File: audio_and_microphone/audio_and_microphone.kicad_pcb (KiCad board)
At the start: 2 copper layers, 14 parts

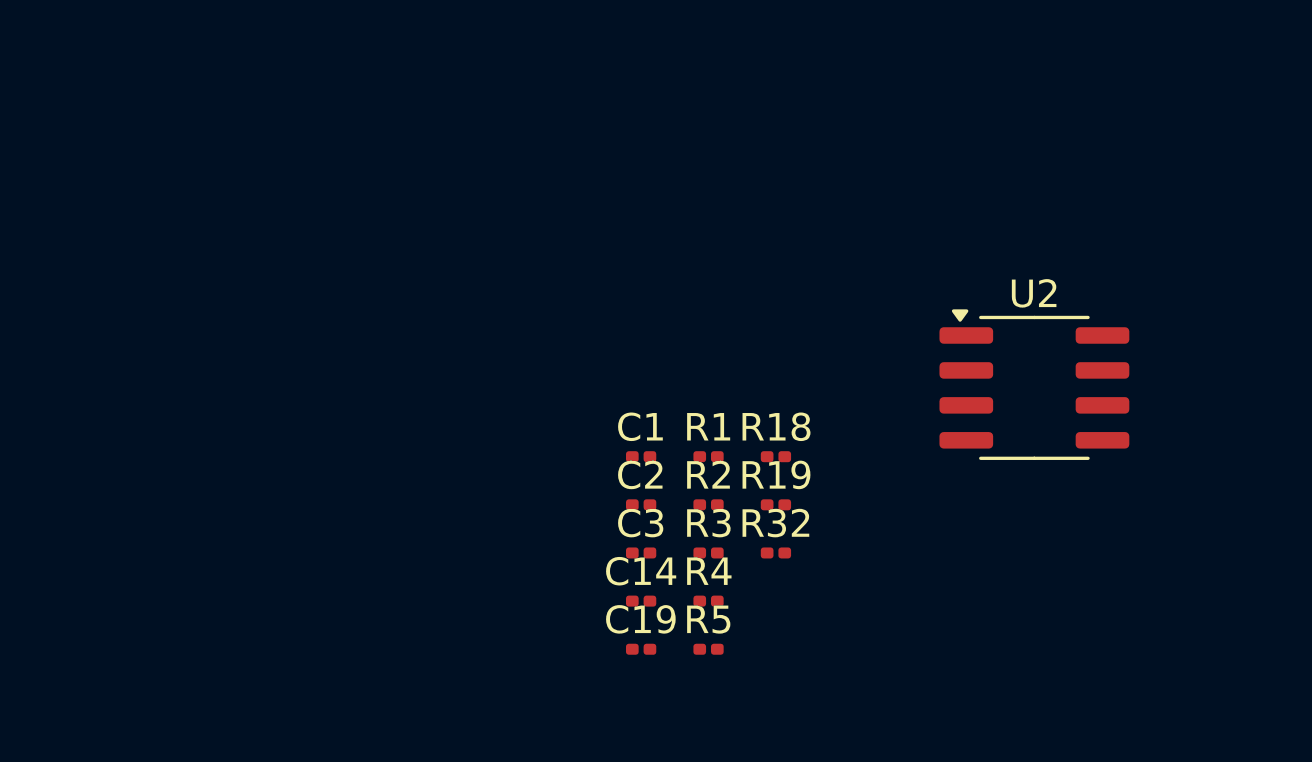
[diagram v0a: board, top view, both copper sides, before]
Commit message: updated footprints and pcb layout without 3.3 V connection
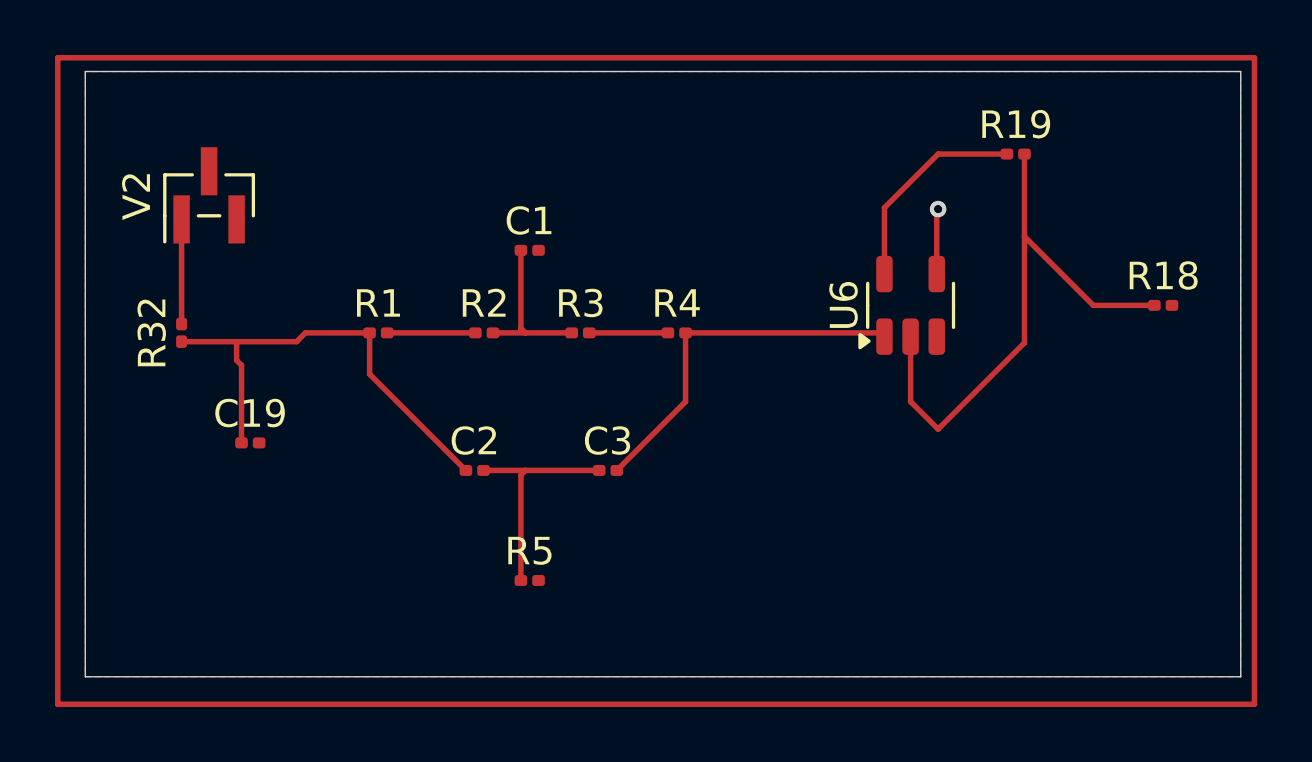
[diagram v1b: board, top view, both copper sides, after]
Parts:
- removed C14: 0.1u, Capacitor_SMD:C_0201_0603Metric
- removed U2: ~, Package_SO:SOIC-8_3.9x4.9mm_P1.27mm
- added U6: ~, Package_TO_SOT_SMD:SOT-23-5, F.Cu at (141.5, 55.5)
- added V2: VPWL, Connector_PinHeader_1.00mm:PinHeader_1x03_P1.00mm_Vertical_SMD_Pin1Left, F.Cu at (116.0, 51.5)
- moved R32 23.0 mm to (115.0, 56.5), turned to 90 degrees
- moved C19 16.1 mm to (117.5, 60.5)
- moved R19 15.4 mm to (145.3, 50.0)
- moved R18 15.1 mm to (150.7, 55.5)
- moved R1 12.8 mm to (122.2, 56.5)
- moved R2 10.3 mm to (126.0, 56.5)
- moved R4 9.82 mm to (133.0, 56.5)
- moved R3 9.26 mm to (129.5, 56.5)
- moved C1 8.52 mm to (127.7, 53.5)
- moved R5 6.96 mm to (127.7, 65.5)
- moved C2 6.18 mm to (125.7, 61.5)
- moved C3 3.23 mm to (130.5, 61.5)
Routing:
- net Net-(U6--): track 0.00 -> 20.8 mm
- net Net-(C19-Pad1): track 0.00 -> 17.2 mm
- net Net-(U6-+): track 0.00 -> 13.3 mm
- net Net-(C2-Pad2): track 0.00 -> 8.27 mm
- net /ENV_OUT: track 0.00 -> 7.67 mm
- net Net-(C1-Pad1): track 0.00 -> 5.93 mm
- net Net-(R32-Pad2): track 0.00 -> 3.80 mm
- net Net-(R1-Pad2): track 0.00 -> 3.21 mm
- net Net-(R3-Pad2): track 0.00 -> 2.86 mm
- net GND: track 0.00 -> 2.38 mm, vias 0 -> 1
- added copper zone on F.Cu, net GND
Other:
- board outline added: 42 x 22 mm

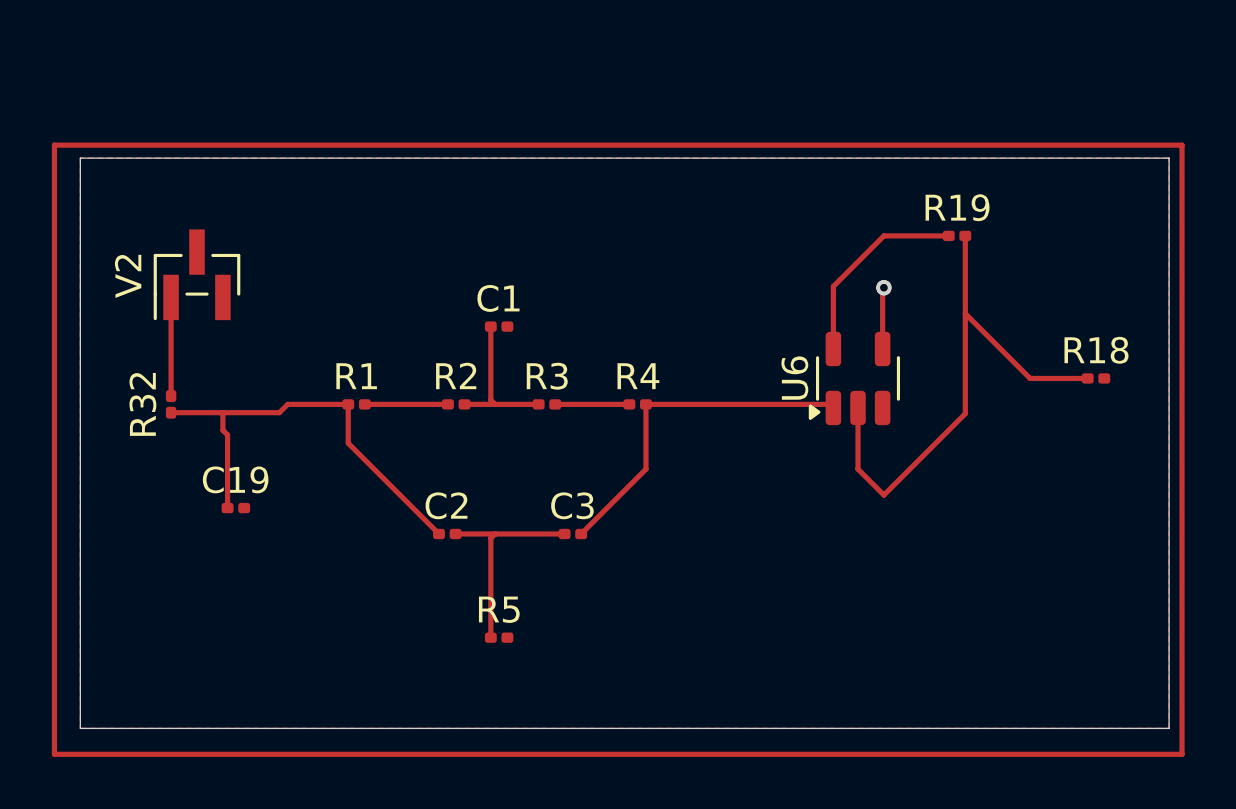
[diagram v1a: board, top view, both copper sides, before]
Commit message: improved pcb space layout
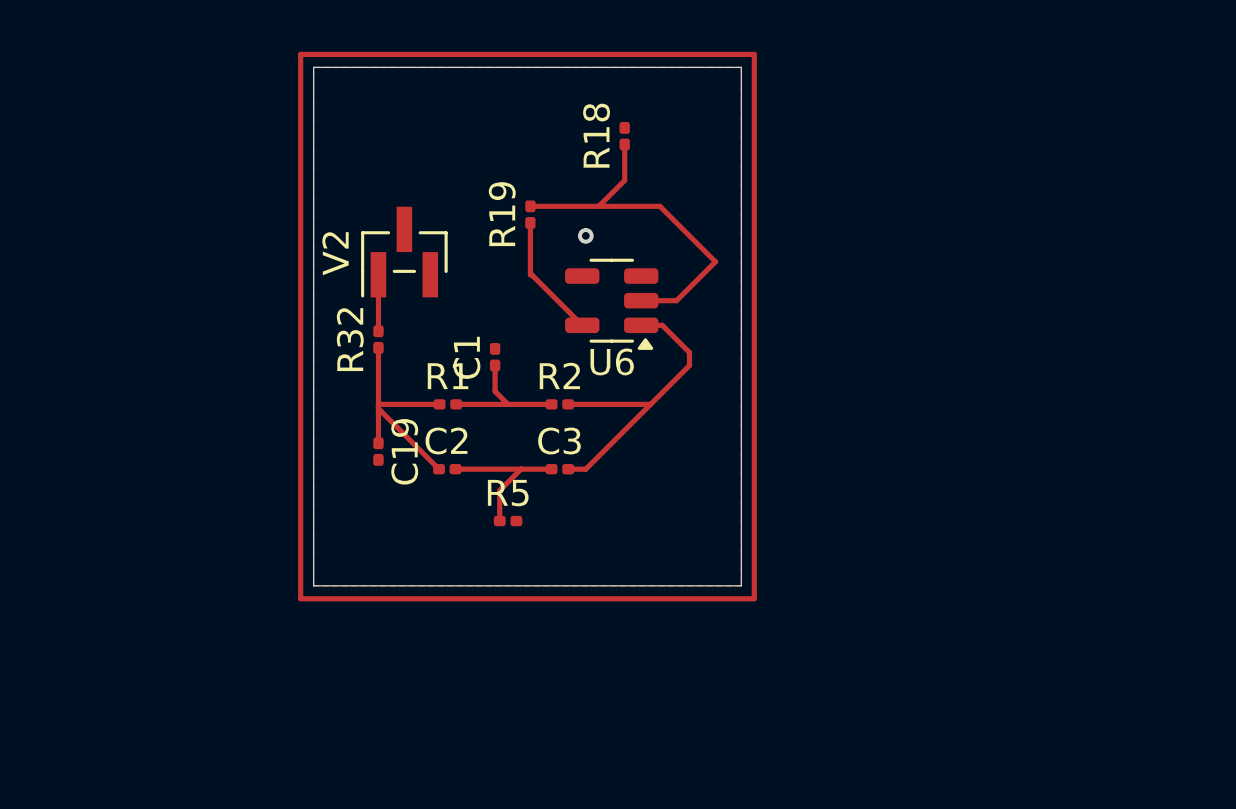
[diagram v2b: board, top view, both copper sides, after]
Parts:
- removed the R2 at (126.0, 56.5)
- removed R3: 4.7k, Resistor_SMD:R_0201_0603Metric
- R1: value 4.7k -> 26.7k
- R2: renamed from R4; value 22k -> 26.7k
- moved R18 20.4 mm to (132.5, 46.2), turned to 90 degrees
- moved R19 16.5 mm to (128.9, 49.2), turned to 90 degrees
- moved U6 9.96 mm to (132.0, 52.5), turned to 180 degrees
- moved R32 8.38 mm to (123.0, 54.0)
- moved V2 8.05 mm to (124.0, 50.6)
- moved C19 5.92 mm to (123.0, 58.3), turned to -90 degrees
- moved R5 4.51 mm to (128.0, 61.0)
- moved R1 3.53 mm to (125.7, 56.5)
- moved R2 3.00 mm to (130.0, 56.5)
- moved C3 2.55 mm to (130.0, 59.0)
- moved C2 2.50 mm to (125.7, 59.0)
- moved C1 1.19 mm to (127.5, 54.7), turned to 90 degrees
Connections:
- R1 pad 2: Net-(R1-Pad2) -> Net-(C1-Pad1)
- R2 pad 1: Net-(R3-Pad2) -> Net-(C1-Pad1)
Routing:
- net Net-(C19-Pad1): track 17.2 -> 9.51 mm
- net Net-(U6--): track 20.8 -> 14.3 mm
- net Net-(R1-Pad2): track 3.21 -> 0.00 mm
- net /ENV_OUT: track 7.67 -> 4.81 mm
- net Net-(R3-Pad2): track 2.86 -> 0.00 mm
- net GND: track 2.38 -> 0.00 mm
- net Net-(C2-Pad2): track 8.27 -> 6.04 mm
- net Net-(R32-Pad2): track 3.80 -> 2.18 mm
- net Net-(U6-+): track 13.3 -> 12.3 mm
- net Net-(C1-Pad1): track 5.93 -> 5.39 mm
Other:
- board size 42 x 22 mm -> 16.5 x 20 mm

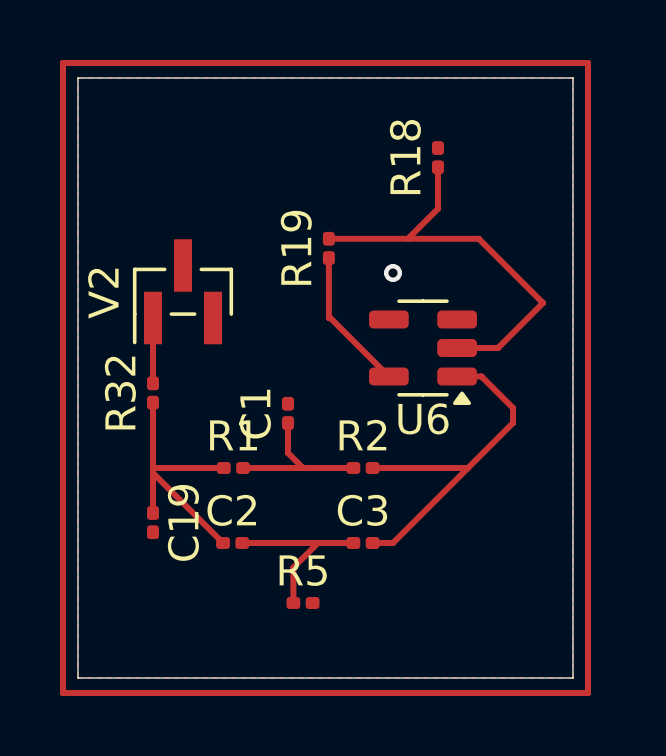
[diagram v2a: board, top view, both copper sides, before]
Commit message: excluded voltage sources from board and replaced with connectors
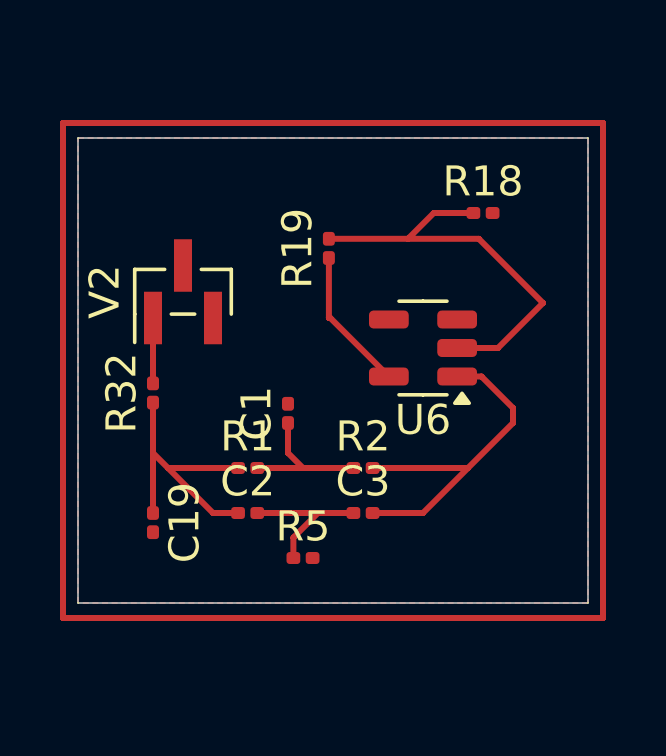
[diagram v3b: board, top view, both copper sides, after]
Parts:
- moved R18 2.38 mm to (134.0, 48.0), turned to 0 degrees
- moved R5 1.50 mm to (128.0, 59.5)
- moved C2 1.12 mm to (126.2, 58.0)
- moved C3 1.00 mm to (130.0, 58.0)
- moved R1 0.47 mm to (126.2, 56.5)
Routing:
- net Net-(C2-Pad2): track 6.04 -> 5.04 mm
- net GND: vias 1 -> 0
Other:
- board size 16.5 x 20 mm -> 17 x 15.5 mm
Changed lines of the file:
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@@
 	(footprint "Resistor_SMD:R_0201_0603Metric"
 		(layer "F.Cu")
-		(at 132.5 46.155 90)
+		(at 134 48)
 		(descr "Resistor SMD 0201 (0603 Metric), square (rectangular) end terminal, IPC-7351 nominal, (Body size source: https://www.vishay.com/docs/20052/crcw0201e3.pdf), generated with kicad-footprint-generator")
 		(tags "resistor")
 		(property "Reference" "R18"
-			(at 0 -1.05 90)
+			(at 0 -1.05 0)
 			(layer "F.SilkS")
 			(effects
@@
 		)
 		(property "Value" "22K"
-			(at 0 1.05 90)
+			(at 0 1.05 0)
 			(layer "F.Fab")
 			(effects
@@
 		)
 		(property "Datasheet" "~"
-			(at 0 0 90)
+			(at 0 0 0)
 			(layer "F.Fab")
 			(hide yes)
@@
 		)
 		(property "Description" "Resistor, US symbol"
-			(at 0 0 90)
+			(at 0 0 0)
 			(layer "F.Fab")
 			(hide yes)
@@
 		(attr smd)
 		(fp_line
+			(start -0.7 -0.35)
+			(end 0.7 -0.35)
+			(stroke
+				(width 0.05)
+				(type solid)
+			)
+			(layer "F.CrtYd")
+		)
+		(fp_line
+			(start -0.7 0.35)
+			(end -0.7 -0.35)
+			(stroke
+				(width 0.05)
+				(type solid)
+			)
+			(layer "F.CrtYd")
+		)
+		(fp_line
 			(start 0.7 -0.35)
 			(end 0.7 0.35)
@@
 		)
 		(fp_line
-			(start -0.7 -0.35)
-			(end 0.7 -0.35)
-			(stroke
-				(width 0.05)
-				(type solid)
-			)
-			(layer "F.CrtYd")
-		)
-		(fp_line
 			(start 0.7 0.35)
 			(end -0.7 0.35)
@@
 		)
 		(fp_line
-			(start -0.7 0.35)
-			(end -0.7 -0.35)
-			(stroke
-				(width 0.05)
-				(type solid)
-			)
-			(layer "F.CrtYd")
+			(start -0.3 -0.15)
+			(end 0.3 -0.15)
+			(stroke
+				(width 0.1)
+				(type solid)
+			)
+			(layer "F.Fab")
+		)
+		(fp_line
+			(start -0.3 0.15)
+			(end -0.3 -0.15)
+			(stroke
+				(width 0.1)
+				(type solid)
+			)
+			(layer "F.Fab")
 		)
 		(fp_line
@@
 		)
 		(fp_line
-			(start -0.3 -0.15)
-			(end 0.3 -0.15)
-			(stroke
-				(width 0.1)
-				(type solid)
-			)
-			(layer "F.Fab")
-		)
-		(fp_line
 			(start 0.3 0.15)
 			(end -0.3 0.15)
@@
 			(layer "F.Fab")
 		)
-		(fp_line
-			(start -0.3 0.15)
-			(end -0.3 -0.15)
-			(stroke
-				(width 0.1)
-				(type solid)
-			)
-			(layer "F.Fab")
-		)
 		(fp_text user "${REFERENCE}"
-			(at 0 -0.68 90)
+			(at 0 -0.68 0)
 			(layer "F.Fab")
 			(effects
@@
 		)
 		(pad "" smd roundrect
-			(at -0.345 0 90)
+			(at -0.345 0)
 			(size 0.318 0.36)
 			(layers "F.Paste")
@@
 		)
 		(pad "" smd roundrect
-			(at 0.345 0 90)
+			(at 0.345 0)
 			(size 0.318 0.36)
 			(layers "F.Paste")
@@
 		)
 		(pad "1" smd roundrect
-			(at -0.32 0 90)
+			(at -0.32 0)
 			(size 0.46 0.4)
 			(layers "F.Cu" "F.Mask")
@@
 		)
 		(pad "2" smd roundrect
-			(at 0.32 0 90)
+			(at 0.32 0)
 			(size 0.46 0.4)
 			(layers "F.Cu" "F.Mask")
@@
 	(footprint "Resistor_SMD:R_0201_0603Metric"
 		(layer "F.Cu")
-		(at 125.68 56.5)
+		(at 126.155 56.5)
 		(descr "Resistor SMD 0201 (0603 Metric), square (rectangular) end terminal, IPC-7351 nominal, (Body size source: https://www.vishay.com/docs/20052/crcw0201e3.pdf), generated with kicad-footprint-generator")
 		(tags "resistor")
@@
 	(footprint "Resistor_SMD:R_0201_0603Metric"
 		(layer "F.Cu")
-		(at 128 61)
+		(at 128 59.5)
 		(descr "Resistor SMD 0201 (0603 Metric), square (rectangular) end terminal, IPC-7351 nominal, (Body size source: https://www.vishay.com/docs/20052/crcw0201e3.pdf), generated with kicad-footprint-generator")
 		(tags "resistor")
@@
 	(footprint "Capacitor_SMD:C_0201_0603Metric"
 		(layer "F.Cu")
-		(at 130 59)
+		(at 130 58)
 		(descr "Capacitor SMD 0201 (0603 Metric), square (rectangular) end terminal, IPC-7351 nominal, (Body size source: https://www.vishay.com/docs/20052/crcw0201e3.pdf), generated with kicad-footprint-generator")
 		(tags "capacitor")
@@
 	(footprint "Capacitor_SMD:C_0201_0603Metric"
 		(layer "F.Cu")
-		(at 125.655 59)
+		(at 126.155 58)
 		(descr "Capacitor SMD 0201 (0603 Metric), square (rectangular) end terminal, IPC-7351 nominal, (Body size source: https://www.vishay.com/docs/20052/crcw0201e3.pdf), generated with kicad-footprint-generator")
 		(tags "capacitor")
@@
 	)
 	(gr_rect
-		(start 120 43)
-		(end 137.5 64)
+		(start 120 45)
+		(end 138 61.5)
 		(stroke
 			(width 0.2)
@@
 	)
 	(gr_rect
-		(start 120.5 43.5)
-		(end 137 63.5)
+		(start 120.5 45.5)
+		(end 137.5 61)
 		(stroke
 			(width 0.05)
@@
 		(layer "Edge.Cuts")
 	)
-	(via
-		(at 131 50)
-		(size 0.6)
-		(drill 0.3)
-		(layers "F.Cu" "B.Cu")
-		(free yes)
-		(net 1)
-	)
 	(segment
 		(start 127.5 56)
@@
 	)
 	(segment
-		(start 128 56.5)
-		(end 126 56.5)
+		(start 126.475 56.5)
+		(end 128 56.5)
 		(width 0.2)
 		(layer "F.Cu")
@@
 	)
 	(segment
-		(start 123 56.5)
-		(end 125.36 56.5)
+		(start 123 56)
+		(end 123 56.5)
 		(width 0.2)
 		(layer "F.Cu")
@@
 	)
 	(segment
-		(start 125.335 59)
-		(end 123 56.665)
+		(start 125.835 56.5)
+		(end 123.5 56.5)
 		(width 0.2)
 		(layer "F.Cu")
@@
 	)
 	(segment
+		(start 123.5 56.5)
+		(end 123 56)
+		(width 0.2)
+		(layer "F.Cu")
+		(net 3)
+	)
+	(segment
 		(start 123 54.32)
-		(end 123 56.5)
+		(end 123 55.5)
 		(width 0.2)
 		(layer "F.Cu")
@@
 	)
 	(segment
-		(start 128.5 59)
-		(end 129.68 59)
+		(start 125 58)
+		(end 123.5 56.5)
+		(width 0.2)
+		(layer "F.Cu")
+		(net 3)
+	)
+	(segment
+		(start 123 55.5)
+		(end 123 56)
+		(width 0.2)
+		(layer "F.Cu")
+		(net 3)
+	)
+	(segment
+		(start 125.835 58)
+		(end 125 58)
+		(width 0.2)
+		(layer "F.Cu")
+		(net 3)
+	)
+	(segment
+		(start 127.68 59.5)
+		(end 127.68 58.82)
 		(width 0.2)
 		(layer "F.Cu")
@@
 	)
 	(segment
-		(start 127.68 61)
-		(end 127.68 59.82)
+		(start 127.68 58.82)
+		(end 128.5 58)
 		(width 0.2)
 		(layer "F.Cu")
@@
 	)
 	(segment
-		(start 125.975 59)
-		(end 128.5 59)
+		(start 128.5 58)
+		(end 129.68 58)
 		(width 0.2)
 		(layer "F.Cu")
@@
 	)
 	(segment
-		(start 127.68 59.82)
-		(end 128.5 59)
+		(start 126.475 58)
+		(end 128.5 58)
 		(width 0.2)
 		(layer "F.Cu")
@@
 	)
 	(segment
-		(start 131 59)
+		(start 130.32 58)
+		(end 132 58)
+		(width 0.2)
+		(layer "F.Cu")
+		(net 5)
+	)
+	(segment
+		(start 132 58)
 		(end 133.5 56.5)
-		(width 0.2)
-		(layer "F.Cu")
-		(net 5)
-	)
-	(segment
-		(start 130.32 59)
-		(end 131 59)
 		(width 0.2)
 		(layer "F.Cu")
@@
 	)
 	(segment
-		(start 132.5 47.86)
-		(end 132.5 46.475)
-		(width 0.2)
-		(layer "F.Cu")
-		(net 7)
-	)
-	(segment
 		(start 136 51)
 		(end 133.86 48.86)
@@
 	)
 	(segment
-		(start 131.5 48.86)
-		(end 132.5 47.86)
+		(start 133.68 48)
+		(end 132.36 48)
 		(width 0.2)
 		(layer "F.Cu")
@@
 		(start 134.5 52.5)
 		(end 136 51)
+		(width 0.2)
+		(layer "F.Cu")
+		(net 7)
+	)
+	(segment
+		(start 132.36 48)
+		(end 131.5 48.86)
 		(width 0.2)
 		(layer "F.Cu")
@@
 		(polygon
 			(pts
-				(xy 120.5 43.5) (xy 137 43.5) (xy 137 63.5) (xy 120.5 63.5)
-			)
-		)
+				(xy 120.5 45.5) (xy 137.5 45.5) (xy 137.5 61) (xy 120.5 61)
+			)
+		)
